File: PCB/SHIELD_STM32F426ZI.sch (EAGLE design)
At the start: 1 part, among them U1 NUCLEO-F429ZI

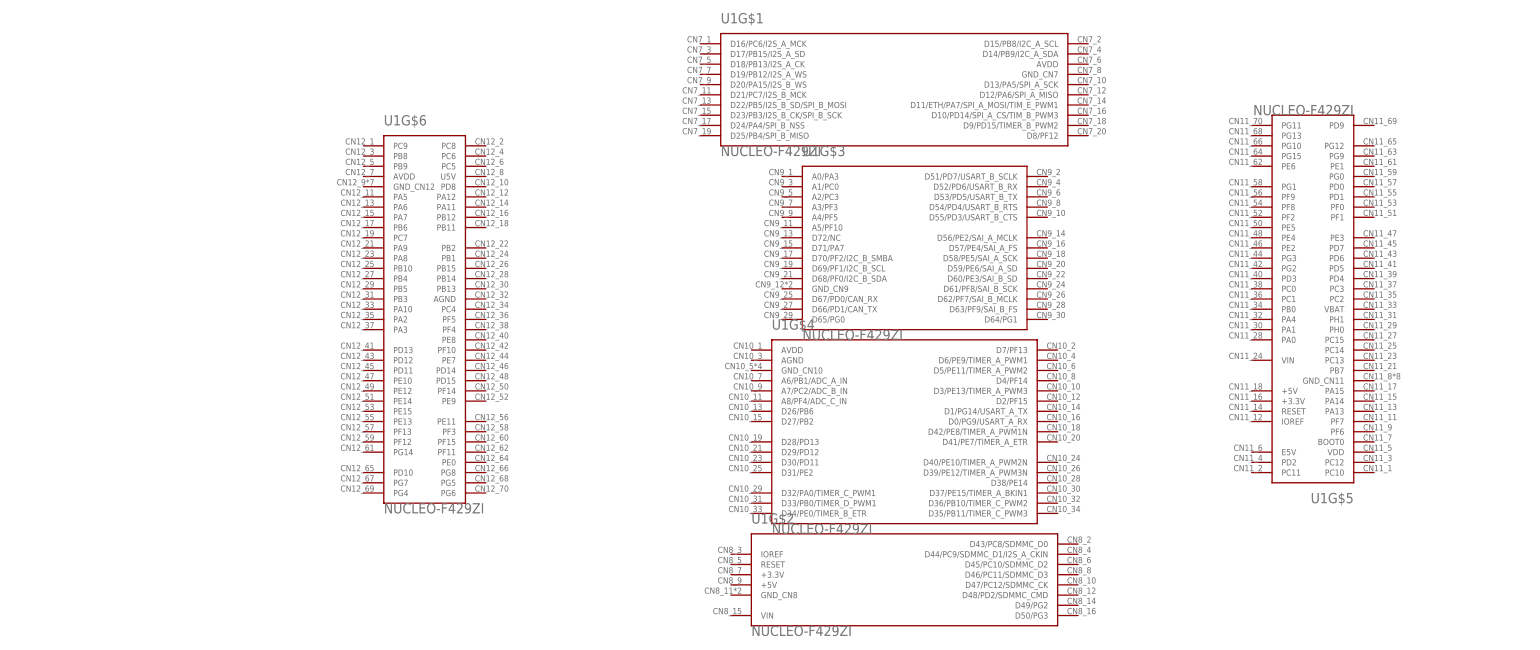
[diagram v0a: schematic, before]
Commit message: new fmc pin
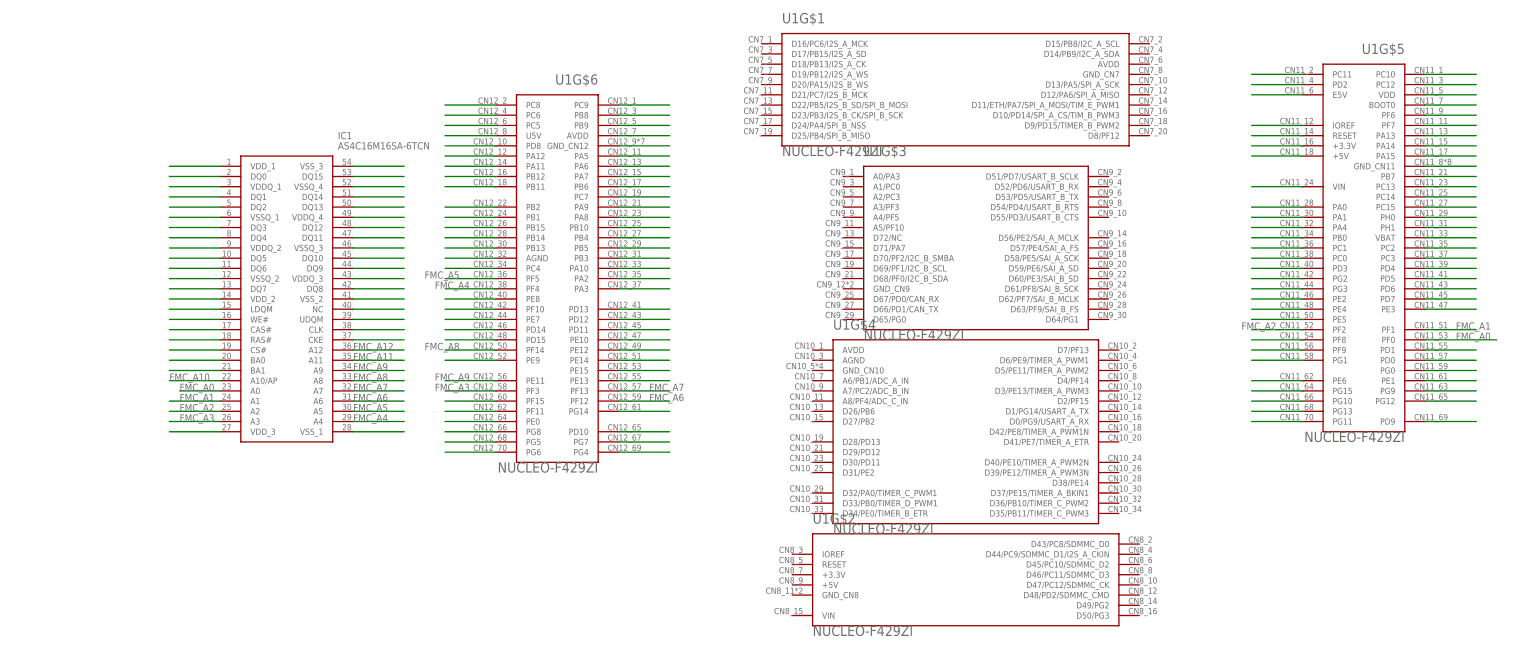
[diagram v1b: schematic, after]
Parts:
- added IC1: AS4C16M16SA-6TCN, sdram:AS4C16M16SA-6TCN
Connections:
- new net FMC_A0: IC1.A0, U1G$5.PF0
- new net FMC_A1: IC1.A1, U1G$5.PF1
- new net FMC_A10: IC1.A10/AP
- new net FMC_A11: IC1.A11
- new net FMC_A12: IC1.A12
- new net FMC_A2: IC1.A2, U1G$5.PF2
- new net FMC_A3: IC1.A3, U1G$6.PF3
- new net FMC_A4: IC1.A4, U1G$6.PF4
- new net FMC_A5: IC1.A5, U1G$6.PF5
- new net FMC_A6: IC1.A6, U1G$6.PF12
- new net FMC_A7: IC1.A7, U1G$6.PF13
- new net FMC_A8: IC1.A8, U1G$6.PF14
- new net FMC_A9: IC1.A9, U1G$6.PF15
- new net N$1: IC1.VDD_1
- new net N$10: IC1.DQ5
- new net N$100: U1G$5.PD0
- new net N$101: U1G$5.PG1
- new net N$102: U1G$5.PG0
- new net N$103: U1G$5.PE1
- new net N$104: U1G$5.PE6
- new net N$105: U1G$5.PG9
- new net N$106: U1G$5.PG15
- new net N$107: U1G$5.PG12
- new net N$108: U1G$5.PG10
- new net N$109: U1G$5.PG13
- new net N$11: IC1.DQ6
- new net N$110: U1G$5.PD9
- new net N$111: U1G$5.PG11
- new net N$112: U1G$6.PA12
- new net N$113: U1G$6.PA6
- new net N$114: U1G$6.PA11
- new net N$115: U1G$6.PA7
- new net N$116: U1G$6.PB12
- new net N$117: U1G$6.PB6
- new net N$118: U1G$6.PB11
- new net N$119: U1G$6.PC7
- new net N$12: IC1.VSSQ_2
- new net N$120: U1G$6.PA9
- new net N$121: U1G$6.PB2
- new net N$122: U1G$6.PA8
- new net N$123: U1G$6.PB1
- new net N$124: U1G$6.PB10
- new net N$125: U1G$6.PB15
- new net N$126: U1G$6.PB4
- new net N$127: U1G$6.PB14
- new net N$128: U1G$6.PB5
- new net N$129: U1G$6.PB13
- new net N$13: IC1.DQ7
- new net N$130: U1G$6.PB3
- new net N$131: U1G$6.AGND
- new net N$132: U1G$6.PA10
- new net N$133: U1G$6.PC4
- new net N$134: U1G$6.PA2
- new net N$136: U1G$6.PA3
- new net N$138: U1G$6.PE8
- new net N$139: U1G$6.PD13
- new net N$14: IC1.VDD_2
- new net N$140: U1G$6.PF10
- new net N$141: U1G$6.PD12
- new net N$142: U1G$6.PE7
- new net N$143: U1G$6.PD11
- new net N$144: U1G$6.PD14
- new net N$145: U1G$6.PE10
- new net N$146: U1G$6.PD15
- new net N$147: U1G$6.PE12
- new net N$149: U1G$6.PE14
- new net N$15: IC1.LDQM
- new net N$150: U1G$6.PE9
- new net N$151: U1G$6.PE15
- new net N$152: U1G$6.PE13
- new net N$153: U1G$6.PE11
- new net N$158: U1G$6.PG14
- new net N$159: U1G$6.PF11
- new net N$16: IC1.WE#
- new net N$160: U1G$6.PE0
- new net N$161: U1G$6.PD10
- new net N$162: U1G$6.PG8
- new net N$163: U1G$6.PG7
- new net N$164: U1G$6.PG5
- new net N$165: U1G$6.PG4
- new net N$166: U1G$6.PG6
- new net N$17: IC1.CAS#
- new net N$18: IC1.RAS#
- new net N$19: IC1.CS#
- new net N$2: IC1.DQ0
- new net N$20: IC1.BA0
- new net N$21: IC1.BA1
- new net N$22: U1G$6.PC9
- new net N$23: U1G$5.PC10
- new net N$24: U1G$5.PC11
- new net N$25: U1G$5.PC12
- new net N$26: IC1.VDD_3
- new net N$27: IC1.VSS_3
- new net N$28: IC1.DQ15
- new net N$29: IC1.VSSQ_4
- new net N$3: IC1.VDDQ_1
- new net N$30: IC1.DQ14
- new net N$31: IC1.DQ13
- new net N$32: IC1.VDDQ_4
- new net N$33: IC1.DQ12
- new net N$34: IC1.DQ11
- new net N$35: IC1.VSSQ_3
- new net N$36: IC1.DQ10
- new net N$37: IC1.DQ9
- new net N$38: IC1.VDDQ_3
- new net N$39: IC1.DQ8
- new net N$4: IC1.DQ1
- new net N$40: IC1.VSS_2
- new net N$41: IC1.NC
- new net N$42: IC1.UDQM
- new net N$43: IC1.CLK
- new net N$44: IC1.CKE
- new net N$45: U1G$6.PC8
- new net N$46: U1G$6.PB8
- new net N$47: U1G$6.PC6
- new net N$48: U1G$6.PB9
- new net N$49: U1G$6.PC5
- new net N$5: IC1.DQ2
- new net N$50: U1G$6.AVDD
- new net N$51: U1G$6.U5V
- new net N$52: U1G$6.GND_CN12
- new net N$53: IC1.VSS_1
- new net N$54: U1G$5.PD2
- new net N$55: U1G$5.VDD
- new net N$56: U1G$5.E5V
- new net N$57: U1G$5.BOOT0
- new net N$58: U1G$5.PF6
- new net N$59: U1G$5.PF7
- new net N$6: IC1.VSSQ_1
- new net N$60: U1G$5.IOREF
- new net N$61: U1G$5.PA13
- new net N$62: U1G$5.RESET
- new net N$63: U1G$5.PA14
- new net N$64: U1G$5.+3.3V
- new net N$65: U1G$5.PA15
- new net N$66: U1G$5.+5V
- new net N$67: U1G$5.GND_CN11
- new net N$68: U1G$5.PB7
- new net N$69: U1G$5.PC13
- new net N$7: IC1.DQ3
- new net N$70: U1G$5.VIN
- new net N$71: U1G$5.PC14
- new net N$72: U1G$5.PC15
- new net N$73: U1G$5.PA0
- new net N$74: U1G$5.PH0
- new net N$75: U1G$5.PA1
- new net N$76: U1G$5.PH1
- new net N$77: U1G$5.PA4
- new net N$78: U1G$5.VBAT
- new net N$79: U1G$5.PB0
- new net N$8: IC1.DQ4
- new net N$80: U1G$5.PC2
- new net N$81: U1G$5.PC1
- new net N$82: U1G$5.PC3
- new net N$83: U1G$5.PC0
- new net N$84: U1G$5.PD4
- new net N$85: U1G$5.PD3
- new net N$86: U1G$5.PD5
- new net N$87: U1G$5.PG2
- new net N$88: U1G$5.PD6
- new net N$89: U1G$5.PG3
- new net N$9: IC1.VDDQ_2
- new net N$90: U1G$5.PD7
- new net N$91: U1G$5.PE2
- new net N$92: U1G$5.PE3
- new net N$93: U1G$5.PE4
- new net N$94: U1G$5.PE5
- new net N$95: U1G$6.PD8
- new net N$96: U1G$6.PA5
- new net N$97: U1G$5.PF8
- new net N$98: U1G$5.PD1
- new net N$99: U1G$5.PF9
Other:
- moved on the sheet: U1G$1, U1G$2, U1G$3, U1G$4, U1G$5, U1G$6

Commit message: sdram und stm32f4 verdrahten
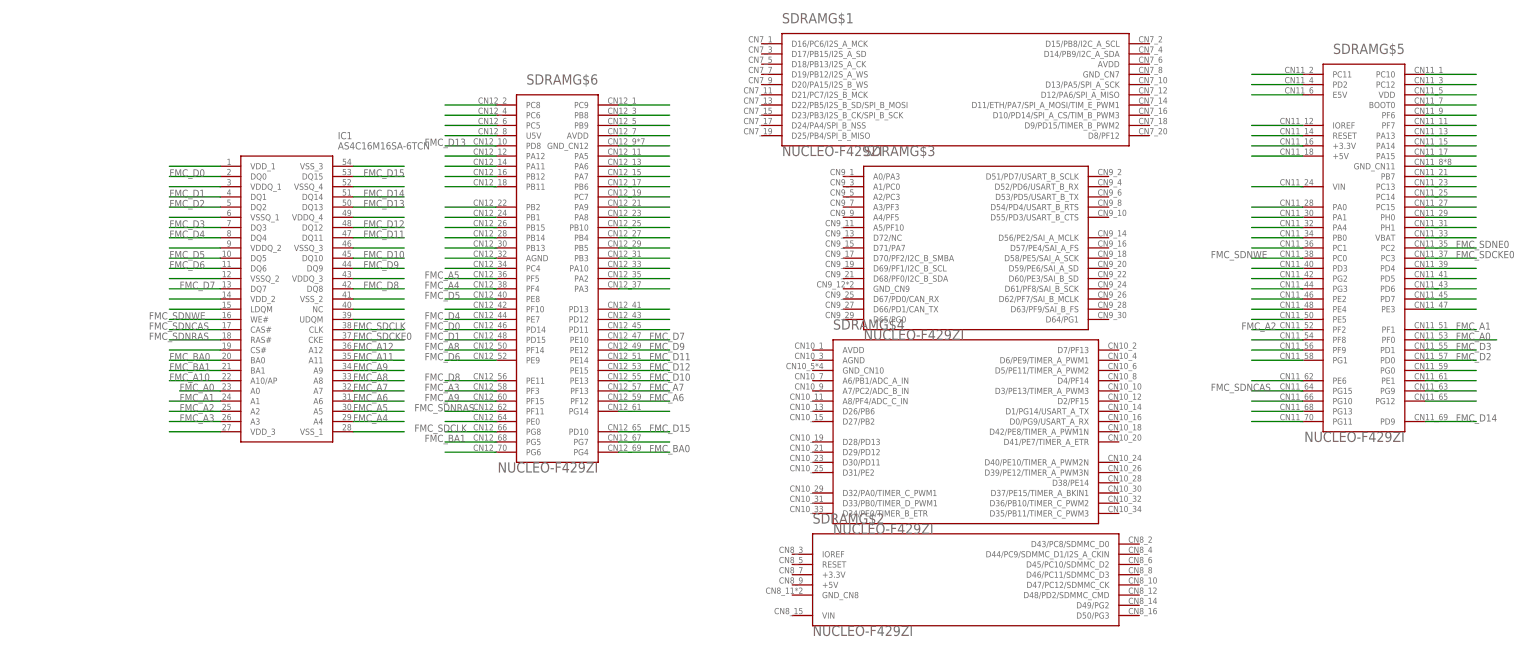
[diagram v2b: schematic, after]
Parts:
- renumbered U1 to SDRAM
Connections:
- net N$80 renamed FMC_SDNE0
- removed net N$10: IC1.DQ5
- removed net N$100: SDRAMG$5.PD0
- removed net N$106: SDRAMG$5.PG15
- removed net N$11: IC1.DQ6
- removed net N$110: SDRAMG$5.PD9
- removed net N$13: IC1.DQ7
- removed net N$138: SDRAMG$6.PE8
- removed net N$142: SDRAMG$6.PE7
- removed net N$144: SDRAMG$6.PD14
- removed net N$145: SDRAMG$6.PE10
- removed net N$146: SDRAMG$6.PD15
- removed net N$147: SDRAMG$6.PE12
- removed net N$149: SDRAMG$6.PE14
- removed net N$150: SDRAMG$6.PE9
- removed net N$151: SDRAMG$6.PE15
- removed net N$152: SDRAMG$6.PE13
- removed net N$153: SDRAMG$6.PE11
- removed net N$159: SDRAMG$6.PF11
- removed net N$16: IC1.WE#
- removed net N$161: SDRAMG$6.PD10
- removed net N$162: SDRAMG$6.PG8
- removed net N$164: SDRAMG$6.PG5
- removed net N$165: SDRAMG$6.PG4
- removed net N$17: IC1.CAS#
- removed net N$18: IC1.RAS#
- removed net N$2: IC1.DQ0
- removed net N$20: IC1.BA0
- removed net N$21: IC1.BA1
- removed net N$28: IC1.DQ15
- removed net N$30: IC1.DQ14
- removed net N$31: IC1.DQ13
- removed net N$33: IC1.DQ12
- removed net N$34: IC1.DQ11
- removed net N$36: IC1.DQ10
- removed net N$37: IC1.DQ9
- removed net N$39: IC1.DQ8
- removed net N$4: IC1.DQ1
- removed net N$43: IC1.CLK
- removed net N$44: IC1.CKE
- removed net N$5: IC1.DQ2
- removed net N$7: IC1.DQ3
- removed net N$8: IC1.DQ4
- removed net N$82: SDRAMG$5.PC3
- removed net N$83: SDRAMG$5.PC0
- removed net N$95: SDRAMG$6.PD8
- removed net N$98: SDRAMG$5.PD1
- new net FMC_BA0: IC1.BA0, SDRAMG$6.PG4
- new net FMC_BA1: IC1.BA1, SDRAMG$6.PG5
- new net FMC_D0: IC1.DQ0, SDRAMG$6.PD14
- new net FMC_D1: IC1.DQ1, SDRAMG$6.PD15
- new net FMC_D10: IC1.DQ10, SDRAMG$6.PE13
- new net FMC_D11: IC1.DQ11, SDRAMG$6.PE14
- new net FMC_D12: IC1.DQ12, SDRAMG$6.PE15
- new net FMC_D13: IC1.DQ13, SDRAMG$6.PD8
- new net FMC_D14: IC1.DQ14, SDRAMG$5.PD9
- new net FMC_D15: IC1.DQ15, SDRAMG$6.PD10
- new net FMC_D2: IC1.DQ2, SDRAMG$5.PD0
- new net FMC_D3: IC1.DQ3, SDRAMG$5.PD1
- new net FMC_D4: IC1.DQ4, SDRAMG$6.PE7
- new net FMC_D5: IC1.DQ5, SDRAMG$6.PE8
- new net FMC_D6: IC1.DQ6, SDRAMG$6.PE9
- new net FMC_D7: IC1.DQ7, SDRAMG$6.PE10
- new net FMC_D8: IC1.DQ8, SDRAMG$6.PE11
- new net FMC_D9: IC1.DQ9, SDRAMG$6.PE12
- new net FMC_SDCKE0: IC1.CKE, SDRAMG$5.PC3
- new net FMC_SDCLK: IC1.CLK, SDRAMG$6.PG8
- new net FMC_SDNCAS: IC1.CAS#, SDRAMG$5.PG15
- new net FMC_SDNRAS: IC1.RAS#, SDRAMG$6.PF11
- new net FMC_SDNWE: IC1.WE#, SDRAMG$5.PC0

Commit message: new with sdramm and sdcard
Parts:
- added C18: 0.1uF, rcl:C-EUC0402K
- added J1: 104239-1430, SamacSys_Parts:104239-1430
- added JP1: (no value), pinhead:PINHD-2X9
- added JP2, JP3: (no value), pinhead:PINHD-1X2
- added R26, R27, R28, R29, R30, R31: 100k, rcl:R-EU_R0402
- renumbered SDRAM to STM32F4
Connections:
- removed net N$1: IC1.VDD_1
- removed net N$101: STM32F4G$5.PG1
- removed net N$102: STM32F4G$5.PG0
- removed net N$104: STM32F4G$5.PE6
- removed net N$105: STM32F4G$5.PG9
- removed net N$113: STM32F4G$6.PA6
- removed net N$117: STM32F4G$6.PB6
- removed net N$119: STM32F4G$6.PC7
- removed net N$12: IC1.VSSQ_2
- removed net N$122: STM32F4G$6.PA8
- removed net N$14: IC1.VDD_2
- removed net N$15: IC1.LDQM
- removed net N$22: STM32F4G$6.PC9
- removed net N$24: STM32F4G$5.PC11
- removed net N$26: IC1.VDD_3
- removed net N$27: IC1.VSS_3
- removed net N$29: IC1.VSSQ_4
- removed net N$3: IC1.VDDQ_1
- removed net N$32: IC1.VDDQ_4
- removed net N$35: IC1.VSSQ_3
- removed net N$38: IC1.VDDQ_3
- removed net N$40: IC1.VSS_2
- removed net N$42: IC1.UDQM
- removed net N$45: STM32F4G$6.PC8
- removed net N$46: STM32F4G$6.PB8
- removed net N$47: STM32F4G$6.PC6
- removed net N$52: STM32F4G$6.GND_CN12
- removed net N$53: IC1.VSS_1
- removed net N$6: IC1.VSSQ_1
- removed net N$64: STM32F4G$5.+3.3V
- removed net N$67: STM32F4G$5.GND_CN11
- removed net N$68: STM32F4G$5.PB7
- removed net N$77: STM32F4G$5.PA4
- removed net N$85: STM32F4G$5.PD3
- removed net N$87: STM32F4G$5.PG2
- removed net N$9: IC1.VDDQ_2
- removed net N$93: STM32F4G$5.PE4
- removed net N$94: STM32F4G$5.PE5
- new net 3.3: JP1.1, JP2.2
- new net 3.3V: C18.1, IC1.VDDQ_1, IC1.VDDQ_2, IC1.VDDQ_3, IC1.VDDQ_4, IC1.VDD_1, IC1.VDD_2, IC1.VDD_3, JP2.1, R26.1, R27.1, R28.1, R29.1, R30.1, R31.1, STM32F4G$5.+3.3V
- new net 3V3: J1.T4_VDD
- new net CARD_DET: J1.S/W_CARD_DETECTOR
- new net DCMI_D0: JP1.16, STM32F4G$6.PC6
- new net DCMI_D1: JP1.15, STM32F4G$6.PC7
- new net DCMI_D2: JP1.14, STM32F4G$6.PC8
- new net DCMI_D3: JP1.13, STM32F4G$6.PC9
- new net DCMI_D4: JP1.12, STM32F4G$5.PE4
- new net DCMI_D5: JP1.11, STM32F4G$5.PD3
- new net DCMI_D6: JP1.10, STM32F4G$5.PE5
- new net DCMI_D7: JP1.9, STM32F4G$5.PE6
- new net DCMI_HSYNC: JP1.6, STM32F4G$5.PA4
- new net DCMI_PIXCK: JP1.7, STM32F4G$6.PA6
- new net DCMI_VSYNC: JP1.5, STM32F4G$5.PG9
- new net GND: C18.2, IC1.VSSQ_1, IC1.VSSQ_2, IC1.VSSQ_3, IC1.VSSQ_4, IC1.VSS_1, IC1.VSS_2, IC1.VSS_3, J1.G1_GND, J1.G2_GND, J1.G3_GND, J1.G4_GND, J1.G5_GND, J1.G6_GND, J1.G7_GND, J1.G8_GND, J1.T6_VSS_(GND), JP1.2, STM32F4G$5.GND_CN11, STM32F4G$6.GND_CN12
- new net I2C1_SCL: JP1.3, STM32F4G$6.PB6
- new net I2C1_SDA: JP1.4, STM32F4G$5.PB7
- new net LDQM: IC1.LDQM, JP3.1
- new net PWDN: JP1.18
- new net RCC_MCO_1: JP1.8, STM32F4G$6.PA8
- new net RESET: JP1.17
- new net SDIO_CK: J1.T5_CLK, R29.2
- new net SDIO_CMD: J1.T3_CMD, R27.2
- new net SDIO_D0: J1.T7_DAT0, R28.2
- new net SDIO_D1: J1.T8_DAT1, R31.2
- new net SDIO_D2: J1.T1_DAT, R26.2
- new net SDIO_D3: J1.T2_CD/DAT3, R30.2
- new net UDQM: IC1.UDQM, JP3.2
- net FMC_A10: now also STM32F4G$5.PG0
- net FMC_A11: now also STM32F4G$5.PG1
- net FMC_A12: now also STM32F4G$5.PG2
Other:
- note added: "CAMERA_MODUL"
- note added: "SDCARD_MODUL"
- note added: "SDRAM_MODUL"
